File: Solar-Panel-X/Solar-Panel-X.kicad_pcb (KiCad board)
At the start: 6 copper layers, 48.4 x 48.4 mm, 81 parts, among them J1 FTS-105-01-L-DV-A, Q1 BSS138DWQ-7, Q2 MBT2222ADW1T1, Q3 BSS138DWQ-7, Q4 MBT2222ADW1T1, U1 BQ25570RGRR, U2 TSL2561

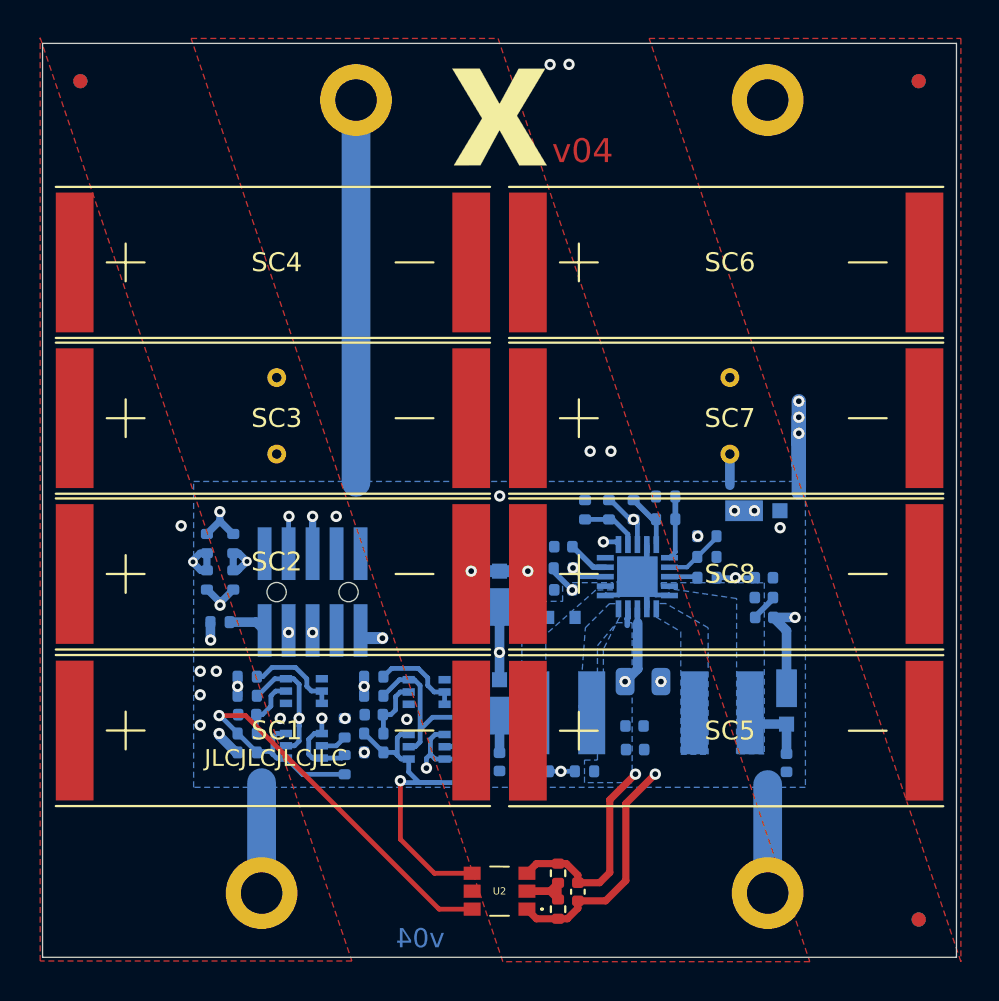
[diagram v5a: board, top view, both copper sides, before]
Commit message: New X board keepouts
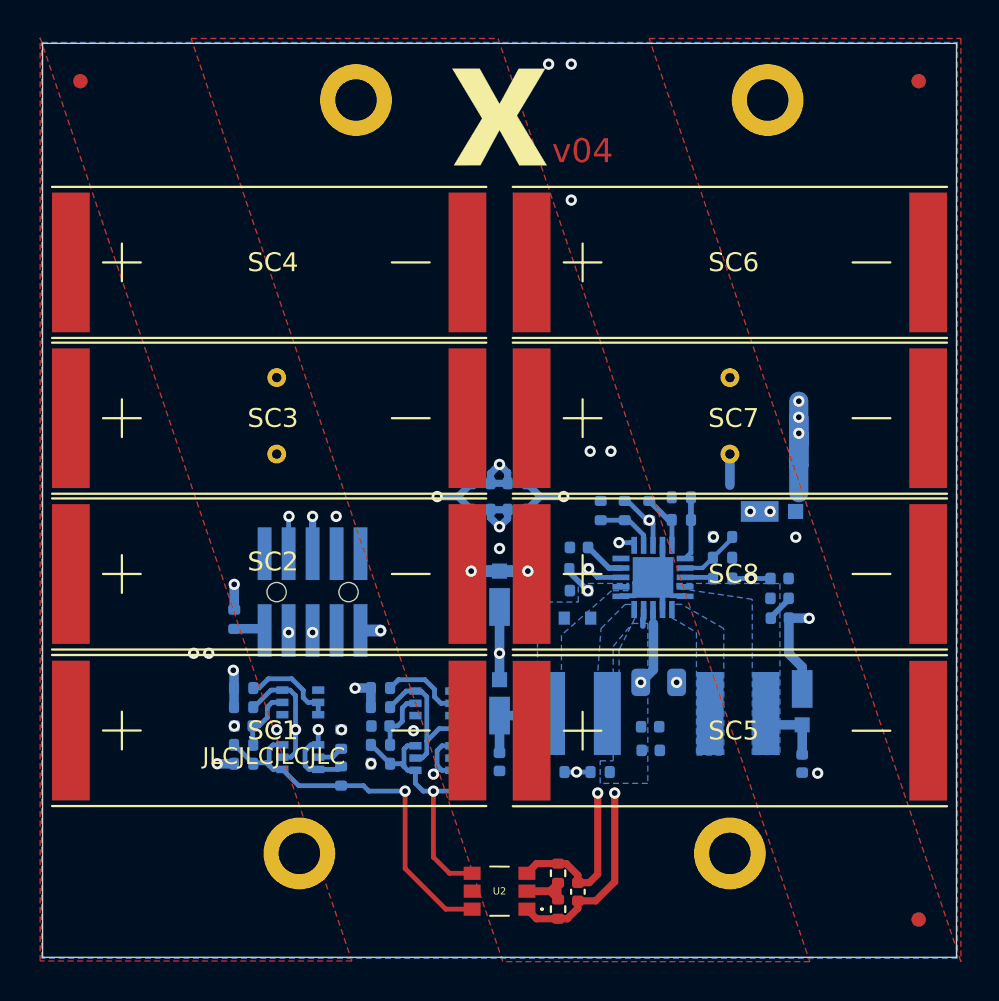
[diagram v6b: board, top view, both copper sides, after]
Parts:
- moved R17 16.7 mm to (107.6, 65.6), turned to 0 degrees
- moved R18 15.4 mm to (105.7, 65.6), turned to 0 degrees
- moved R12 15.1 mm to (107.6, 67.0), turned to 0 degrees
- moved R13 13.6 mm to (105.7, 67.0), turned to 0 degrees
- moved H4 2.90 mm to (118.9, 85.2)
- moved H3 2.90 mm to (96.1, 85.2)
- moved C11 0.83 mm to (121.5, 72.7)
- moved C3 0.83 mm to (110.9, 71.3)
- moved C4 0.83 mm to (110.9, 69.0)
- moved C5 0.83 mm to (115.1, 76.1)
- moved C6 0.83 mm to (121.5, 70.6)
- moved C7 0.83 mm to (114.7, 78.5)
- moved C9 0.83 mm to (114.7, 79.7)
- moved D1 0.83 mm to (110.8, 72.7)
- moved D2 0.83 mm to (122.7, 77.1)
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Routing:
- net GND: track 60.9 -> 26.5 mm
- net /coil: track 13219.8 -> 13247.3 mm
- net COIL_P: track 9.08 -> 17.3 mm
- net SDA_LS: track 27.3 -> 20.3 mm
- net SCL_LS: track 18.5 -> 14.5 mm
- net COIL_N: track 13.3 -> 17.1 mm
- net VBAT: track 46.1 -> 47.3 mm
- net Net-(D3-Pad1): track 13.5 -> 14.4 mm
- net +3V3: track 29.6 -> 28.8 mm
- net SDA2: track 9.76 -> 10.3 mm
- added copper zone on In1.Cu, net +3V3
- added copper zone on In4.Cu, net GND

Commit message: Re-distribute buses between layers
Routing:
- net +3V3: track 28.8 -> 21.9 mm
- net VBAT: track 47.3 -> 41.7 mm
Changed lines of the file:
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@@
   (via (at 91.75 80.45) (size 0.6) (drill 0.3) (layers "F.Cu" "B.Cu") (net 2))
   (via (at 99.05 76.45) (size 0.6) (drill 0.3) (layers "F.Cu" "B.Cu") (net 2))
-  (segment (start 92.3 62.6) (end 92.3 65.8) (width 0.381) (layer "In2.Cu") (net 2))
-  (segment (start 94.9 60) (end 92.3 62.6) (width 0.381) (layer "In2.Cu") (net 2))
   (segment (start 91.75 80.45) (end 92.2 80.45) (width 0.508) (layer "In2.Cu") (net 2))
   (segment (start 123.08963 72.73963) (end 123.1 72.75) (width 0.508) (layer "B.Cu") (net 2))
@@
   (via (at 120.02924 70.63963) (size 0.6) (drill 0.3) (layers "F.Cu" "B.Cu") (net 5))
   (via (at 113.02924 68.73963) (size 0.6) (drill 0.3) (layers "F.Cu" "B.Cu") (net 5))
-  (segment (start 120.02924 70.63963) (end 114.92924 70.63963) (width 0.254) (layer "In4.Cu") (net 5))
-  (segment (start 114.92924 70.63963) (end 113.02924 68.73963) (width 0.254) (layer "In4.Cu") (net 5))
+  (segment (start 120.02924 70.63963) (end 114.92924 70.63963) (width 0.254) (layer "In2.Cu") (net 5))
+  (segment (start 114.92924 70.63963) (end 113.02924 68.73963) (width 0.254) (layer "In2.Cu") (net 5))
   (segment (start 120.02924 70.63963) (end 121.04924 70.63963) (width 0.254) (layer "B.Cu") (net 5))
   (segment (start 113.687849 68.73963) (end 113.02924 68.73963) (width 0.254) (layer "B.Cu") (net 5))
@@
   (via (at 114.62924 67.54963) (size 0.6) (drill 0.3) (layers "F.Cu" "B.Cu") (net 15))
   (via (at 118.02924 68.43963) (size 0.6) (drill 0.3) (layers "F.Cu" "B.Cu") (net 15))
-  (segment (start 115.51924 68.43963) (end 118.02924 68.43963) (width 0.254) (layer "In4.Cu") (net 15))
-  (segment (start 114.62924 67.54963) (end 115.51924 68.43963) (width 0.254) (layer "In4.Cu") (net 15))
+  (segment (start 115.51924 68.43963) (end 118.02924 68.43963) (width 0.254) (layer "In2.Cu") (net 15))
+  (segment (start 114.62924 67.54963) (end 115.51924 68.43963) (width 0.254) (layer "In2.Cu") (net 15))
   (segment (start 114.830005 68.881786) (end 114.830005 67.750395) (width 0.254) (layer "B.Cu") (net 15))
   (segment (start 114.49963 67.54963) (end 113.47963 66.52963) (width 0.254) (layer "B.Cu") (net 15))
@@
   (via (at 111.41924 70.11963) (size 0.6) (drill 0.3) (layers "F.Cu" "B.Cu") (net 20))
   (via (at 110.77924 80.88963) (size 0.6) (drill 0.3) (layers "F.Cu" "B.Cu") (net 20))
-  (segment (start 111.41924 70.11963) (end 110.32924 71.20963) (width 0.254) (layer "In4.Cu") (net 20))
-  (segment (start 110.32924 80.43963) (end 110.77924 80.88963) (width 0.254) (layer "In4.Cu") (net 20))
-  (segment (start 110.32924 71.20963) (end 110.32924 80.43963) (width 0.254) (layer "In4.Cu") (net 20))
+  (segment (start 111.41924 70.11963) (end 110.32924 71.20963) (width 0.254) (layer "In2.Cu") (net 20))
+  (segment (start 110.32924 80.43963) (end 110.77924 80.88963) (width 0.254) (layer "In2.Cu") (net 20))
+  (segment (start 110.32924 71.20963) (end 110.32924 80.43963) (width 0.254) (layer "In2.Cu") (net 20))
   (segment (start 111.41924 70.11963) (end 111.881396 70.581786) (width 0.254) (layer "B.Cu") (net 20))
   (segment (start 111.881396 70.581786) (end 113.130005 70.581786) (width 0.254) (layer "B.Cu") (net 20))
@@
   (via (at 91.3 74.6) (size 0.6) (drill 0.3) (layers "F.Cu" "B.Cu") (net 23))
   (via (at 90.5 74.6) (size 0.6) (drill 0.3) (layers "F.Cu" "B.Cu") (net 23))
-  (segment (start 90.5 74.6) (end 91.3 74.6) (width 0.508) (layer "In4.Cu") (net 23))
-  (segment (start 91.3 74.6) (end 106.7 74.6) (width 0.508) (layer "In4.Cu") (net 23))
+  (segment (start 90.5 74.6) (end 91.3 74.6) (width 0.508) (layer "In2.Cu") (net 23))
+  (segment (start 91.3 74.6) (end 106.7 74.6) (width 0.508) (layer "In2.Cu") (net 23))
   (segment (start 106.7 74.6) (end 106.7 72.148556) (width 0.508) (layer "B.Cu") (net 23))
   (segment (start 106.7 76) (end 106.7 74.6) (width 0.508) (layer "B.Cu") (net 23))
@@
   (via (at 97.1 78.64) (size 0.6) (drill 0.3) (layers "F.Cu" "B.Cu") (net 27))
   (via (at 95.53 73.5) (size 0.6) (drill 0.3) (layers "F.Cu" "B.Cu") (net 27))
-  (segment (start 97.1 75.07) (end 97.1 78.64) (width 0.254) (layer "In1.Cu") (net 27))
-  (segment (start 95.53 73.5) (end 97.1 75.07) (width 0.254) (layer "In1.Cu") (net 27))
+  (segment (start 97.1 75.07) (end 97.1 78.64) (width 0.254) (layer "In3.Cu") (net 27))
+  (segment (start 95.53 73.5) (end 97.1 75.07) (width 0.254) (layer "In3.Cu") (net 27))
   (segment (start 96.603911 80.75) (end 96.403911 80.55) (width 0.254) (layer "B.Cu") (net 27))
   (segment (start 97.1 78.64) (end 97.1 79.45) (width 0.254) (layer "B.Cu") (net 27))
@@
   (via (at 103.2 81) (size 0.6) (drill 0.3) (layers "F.Cu" "B.Cu") (net 28))
   (via (at 95.55 67.35) (size 0.6) (drill 0.3) (layers "F.Cu" "B.Cu") (net 28))
-  (segment (start 103.2 78.4) (end 96.8 72) (width 0.254) (layer "In1.Cu") (net 28))
-  (segment (start 96.8 68.6) (end 95.55 67.35) (width 0.254) (layer "In1.Cu") (net 28))
-  (segment (start 103.2 81) (end 103.2 78.4) (width 0.254) (layer "In1.Cu") (net 28))
-  (segment (start 96.8 72) (end 96.8 68.6) (width 0.254) (layer "In1.Cu") (net 28))
+  (segment (start 103.2 78.4) (end 96.8 72) (width 0.254) (layer "In3.Cu") (net 28))
+  (segment (start 96.8 68.6) (end 95.55 67.35) (width 0.254) (layer "In3.Cu") (net 28))
+  (segment (start 103.2 81) (end 103.2 78.4) (width 0.254) (layer "In3.Cu") (net 28))
+  (segment (start 96.8 72) (end 96.8 68.6) (width 0.254) (layer "In3.Cu") (net 28))
   (segment (start 95.53 67.37) (end 95.53 69.725) (width 0.254) (layer "B.Cu") (net 28))
   (segment (start 103.2 81) (end 103.4 80.8) (width 0.254) (layer "B.Cu") (net 28))
@@
   (via (at 98.33 78.65) (size 0.6) (drill 0.3) (layers "F.Cu" "B.Cu") (net 35))
   (via (at 95.897991 78.642009) (size 0.6) (drill 0.3) (layers "F.Cu" "B.Cu") (net 35))
-  (segment (start 97.642 77.962) (end 98.33 78.65) (width 0.254) (layer "In3.Cu") (net 35))
-  (segment (start 96.578 77.962) (end 97.642 77.962) (width 0.254) (layer "In3.Cu") (net 35))
-  (segment (start 95.897991 78.642009) (end 96.578 77.962) (width 0.254) (layer "In3.Cu") (net 35))
+  (segment (start 95.897991 78.647991) (end 96.65 79.4) (width 0.254) (layer "In3.Cu") (net 35))
+  (segment (start 96.65 79.4) (end 97.58 79.4) (width 0.254) (layer "In3.Cu") (net 35))
+  (segment (start 97.58 79.4) (end 98.33 78.65) (width 0.254) (layer "In3.Cu") (net 35))
+  (segment (start 95.897991 78.642009) (end 95.897991 78.647991) (width 0.254) (layer "In3.Cu") (net 35))
   (segment (start 95.897991 78.642009) (end 95.897991 79.057991) (width 0.254) (layer "B.Cu") (net 35))
   (segment (start 95.897991 79.85592) (end 95.653911 80.1) (width 0.254) (layer "B.Cu") (net 35))
@@
   (via (at 92.65 70.95) (size 0.6) (drill 0.3) (layers "F.Cu" "B.Cu") (net 40))
   (via (at 114.17924 76.13963) (size 0.6) (drill 0.3) (layers "F.Cu" "B.Cu") (net 40))
-  (segment (start 94.175 74.575) (end 103.425 74.575) (width 0.508) (layer "In3.Cu") (net 40))
   (segment (start 104.3 75.45) (end 104.98963 76.13963) (width 0.508) (layer "In3.Cu") (net 40))
   (segment (start 103.425 74.575) (end 101.7 72.85) (width 0.508) (layer "In3.Cu") (net 40))
-  (segment (start 92.65 73.05) (end 94.175 74.575) (width 0.508) (layer "In3.Cu") (net 40))
+  (segment (start 94.9 64.05) (end 94.7 64.05) (width 0.508) (layer "In3.Cu") (net 40))
   (segment (start 104.3 75.45) (end 103.425 74.575) (width 0.508) (layer "In3.Cu") (net 40))
+  (segment (start 94.7 64.05) (end 92.65 66.1) (width 0.508) (layer "In3.Cu") (net 40))
   (segment (start 99.7 64.05) (end 94.9 64.05) (width 0.508) (layer "In3.Cu") (net 40))
   (segment (start 101.7 66.05) (end 99.7 64.05) (width 0.508) (layer "In3.Cu") (net 40))
-  (segment (start 92.65 70.95) (end 92.65 73.05) (width 0.508) (layer "In3.Cu") (net 40))
+  (segment (start 92.65 66.1) (end 92.65 70.95) (width 0.508) (layer "In3.Cu") (net 40))
   (segment (start 104.98963 76.13963) (end 114.17924 76.13963) (width 0.508) (layer "In3.Cu") (net 40))
   (segment (start 101.7 72.85) (end 101.7 66.05) (width 0.508) (layer "In3.Cu") (net 40))

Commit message: Finished Y- Board
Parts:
- moved R1 40.9 mm to (109.8, 47.3)
- moved C1 40.9 mm to (110.8, 46.4)
- moved R2 40.9 mm to (109.8, 45.4)
- moved U2 40.9 mm to (106.7, 46.4)
- moved REF** 40.5 mm to (106.7, 88.2)
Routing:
- net SCL_LS: track 14.5 -> 56.9 mm, vias 1 -> 2
- net /coil: track 13247.3 -> 13206.6 mm
- net SDA_LS: track 20.3 -> 60.1 mm, vias 1 -> 2
- net GND: track 26.5 -> 28.3 mm
- net +3V3: track 21.9 -> 20.7 mm
